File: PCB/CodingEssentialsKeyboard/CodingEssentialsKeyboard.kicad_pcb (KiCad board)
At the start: 2 copper layers, 8 parts, among them U1 ProMicro

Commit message: feat(pcb): finish the pcb
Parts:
- added M2_1: MountingHole_2.2mm_M2, MountingHole:MountingHole_2.2mm_M2, F.Cu at (109.2, 18.2)
- added M2_2: MountingHole_2.2mm_M2, MountingHole:MountingHole_2.2mm_M2, F.Cu at (166.4, 18.2)
- added M2_3: MountingHole_2.2mm_M2, MountingHole:MountingHole_2.2mm_M2, F.Cu at (109.2, 37.3)
- added M2_4: MountingHole_2.2mm_M2, MountingHole:MountingHole_2.2mm_M2, F.Cu at (166.4, 37.3)
- moved SW_K_2 42.6 mm to (137.8, 27.8)
- moved D_K_1 37.1 mm to (118.8, 40.2)
- moved SW_RST1 36.1 mm to (112.7, 43.0), turned to 90 degrees
- moved SW_K_3 25.5 mm to (156.8, 27.8)
- moved U1 18.9 mm to (99.0, 35.6)
- moved SW_K_1 17.7 mm to (118.8, 27.8)
- moved D_K_2 17.0 mm to (130.7, 40.2)
- moved D_K_3 3.62 mm to (149.7, 40.2)
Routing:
- net VCC: track 0.00 -> 160.1 mm, vias 0 -> 2
- net GND: track 0.00 -> 159.2 mm, vias 0 -> 1
- net col_2: track 0.00 -> 102.0 mm, vias 0 -> 1
- net col_1: track 0.00 -> 75.4 mm, vias 0 -> 1
- net col_0: track 0.00 -> 69.2 mm, vias 0 -> 1
- net row_0: track 0.00 -> 63.8 mm
- net LED_DIN: track 0.00 -> 46.8 mm, vias 0 -> 1
- net Net-(SW_K_1-Pad1): track 0.00 -> 43.0 mm, vias 0 -> 2
- net Net-(D_K_3-Pad2): track 0.00 -> 38.5 mm, vias 0 -> 1
- net Net-(D_K_2-Pad2): track 0.00 -> 37.7 mm, vias 0 -> 1
- net Net-(SW_K_2-Pad1): track 0.00 -> 36.8 mm, vias 0 -> 2
- net Net-(D_K_1-Pad2): track 0.00 -> 33.2 mm, vias 0 -> 1
- net RST: track 0.00 -> 32.3 mm
- net Net-(U1-Pad9): track 0.00 -> 17.0 mm
- net Net-(U1-Pad8): track 0.00 -> 17.0 mm
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- added copper zone on B.Cu, net (none)
- added copper zone on F.Cu, net (none)
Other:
- board outline added: 83 x 36 mm
- board text added: "Coding Essential Keyboard"
- board text added: "Designed by Yuyang Zhang"
- board text added: "Version 1.0"

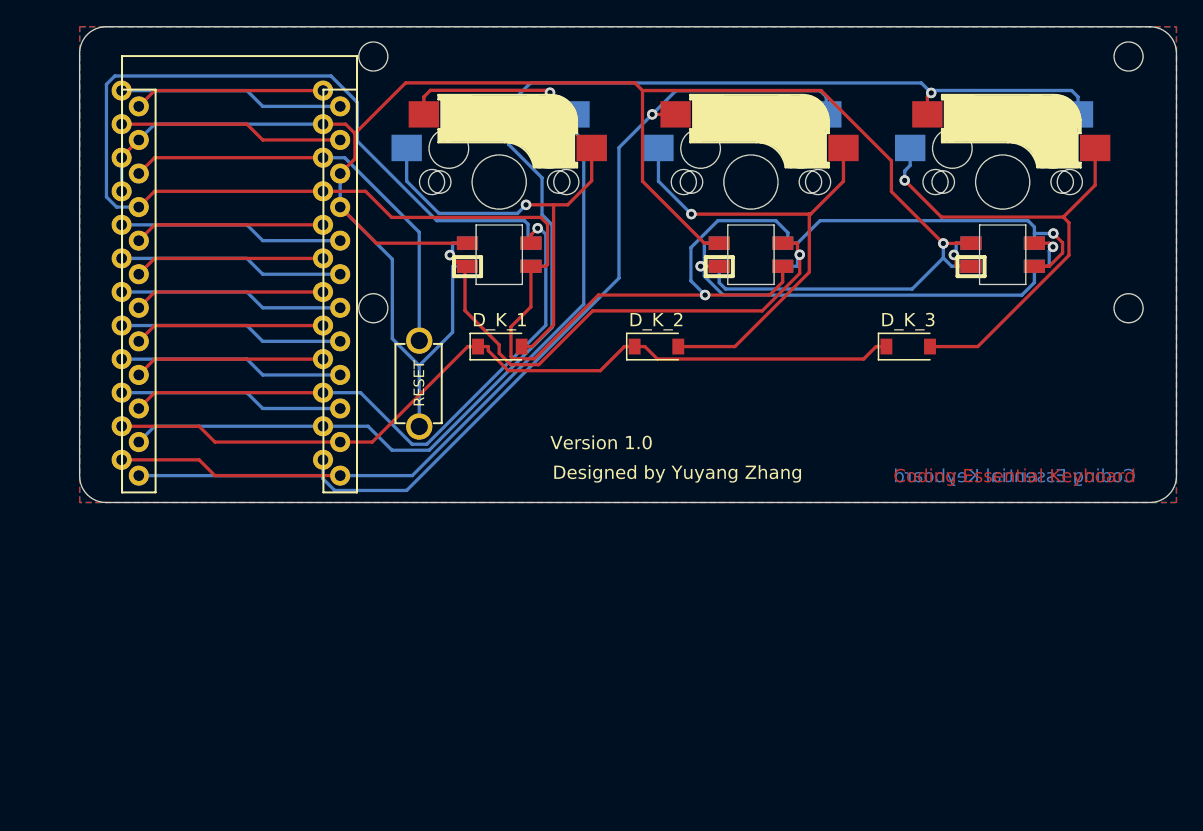
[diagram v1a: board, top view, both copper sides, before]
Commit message: feat(pcb): add top and bottom plate
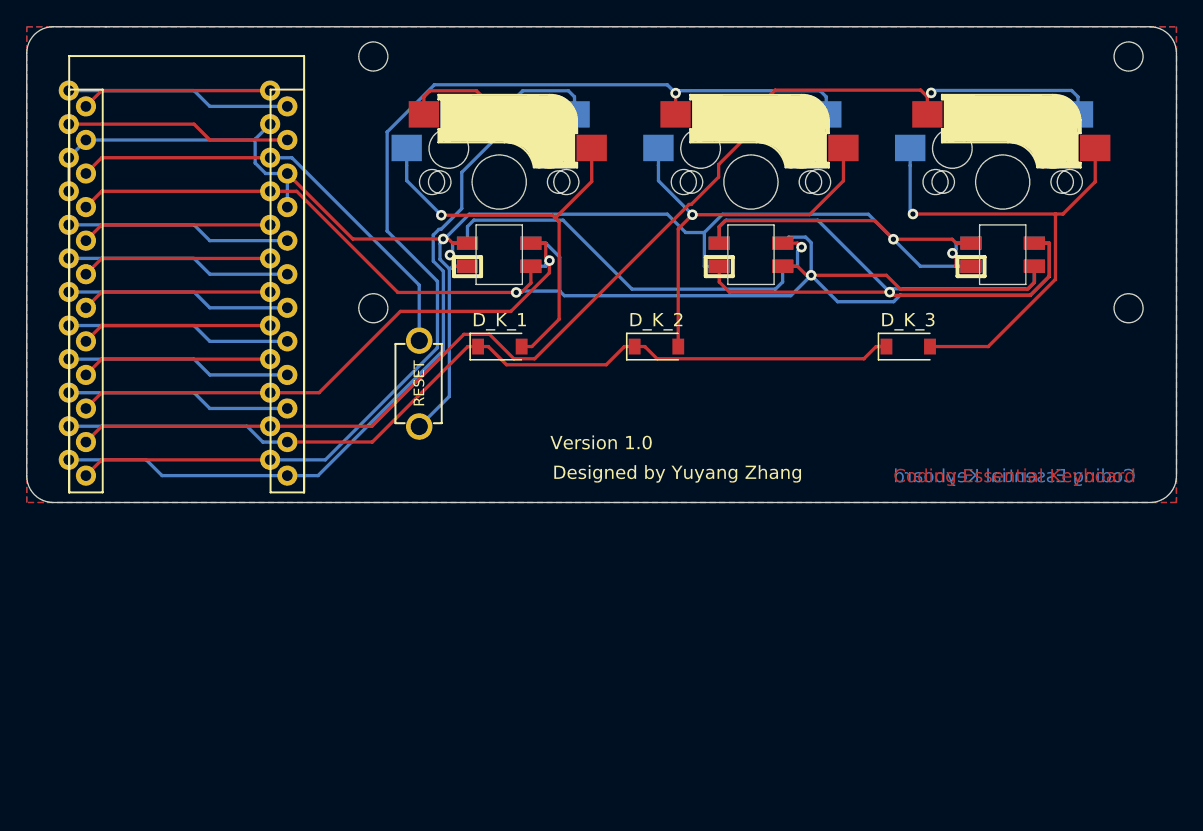
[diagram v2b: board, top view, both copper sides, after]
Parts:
- moved U1 4.00 mm to (95.0, 35.6)
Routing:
- net VCC: track 160.1 -> 116.7 mm
- net GND: track 159.2 -> 127.1 mm, vias 1 -> 2
- net Net-(SW_K_2-Pad1): track 36.8 -> 59.9 mm, vias 2 -> 1
- net col_1: track 75.4 -> 86.7 mm
- net col_2: track 102.0 -> 92.3 mm
- net Net-(D_K_2-Pad2): track 37.7 -> 31.5 mm
- net Net-(SW_K_1-Pad1): track 43.0 -> 37.3 mm
- net row_0: track 63.8 -> 67.3 mm
- net LED_DIN: track 46.8 -> 44.5 mm
- net RST: track 32.3 -> 33.9 mm
- net col_0: track 69.2 -> 70.6 mm
- net Net-(D_K_3-Pad2): track 38.5 -> 39.0 mm
- added copper zone on B.Cu, net GND
- added copper zone on F.Cu, net GND
- removed copper zone on B.Cu, net (none)
- removed copper zone on F.Cu, net (none)
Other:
- board size 83 x 36 mm -> 87 x 36 mm
